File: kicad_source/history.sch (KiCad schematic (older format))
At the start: 0 parts

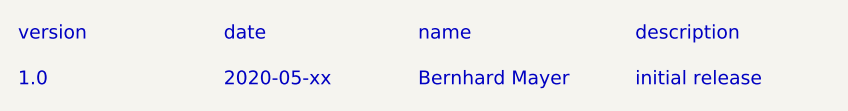
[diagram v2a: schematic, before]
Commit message: added C45 to pin4 of display
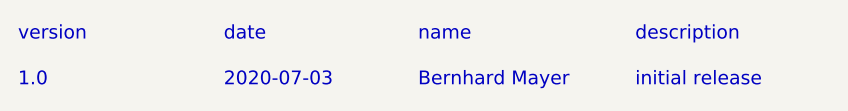
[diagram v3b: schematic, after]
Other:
- note added: "2020-07-03"
- note removed: "2020-05-xx"
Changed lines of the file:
@@
 $Descr A4 11693 8268
 encoding utf-8
-Sheet 6 7
+Sheet 7 7
 Title "history"
-Date "2020-05-13"
+Date "2020-07-03"
 Rev "dev_0.1"
 Comp "generationmake"
@@
 1.0
 Text Notes 1700 1000 0    60   ~ 0
-2020-05-xx
+2020-07-03
 Text Notes 2550 1000 0    60   ~ 0
 Bernhard Mayer
